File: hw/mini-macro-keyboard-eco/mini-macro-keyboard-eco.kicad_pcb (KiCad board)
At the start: 2 copper layers, 59.2 x 30.5 mm, 32 parts, among them J0 USB, J1 DEBUG_SWD, SW1 SW_Cherry_MX_1.00u_PCB, SW2 SW_Cherry_MX_1.00u_PCB, SW3 SW_Cherry_MX_1.00u_PCB, SW5 LAYOUT, SW6 BACKLIGHT, U1 USBLC6-2SC6, U2 XC6206P322MR, U3 STM32F070F6P6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

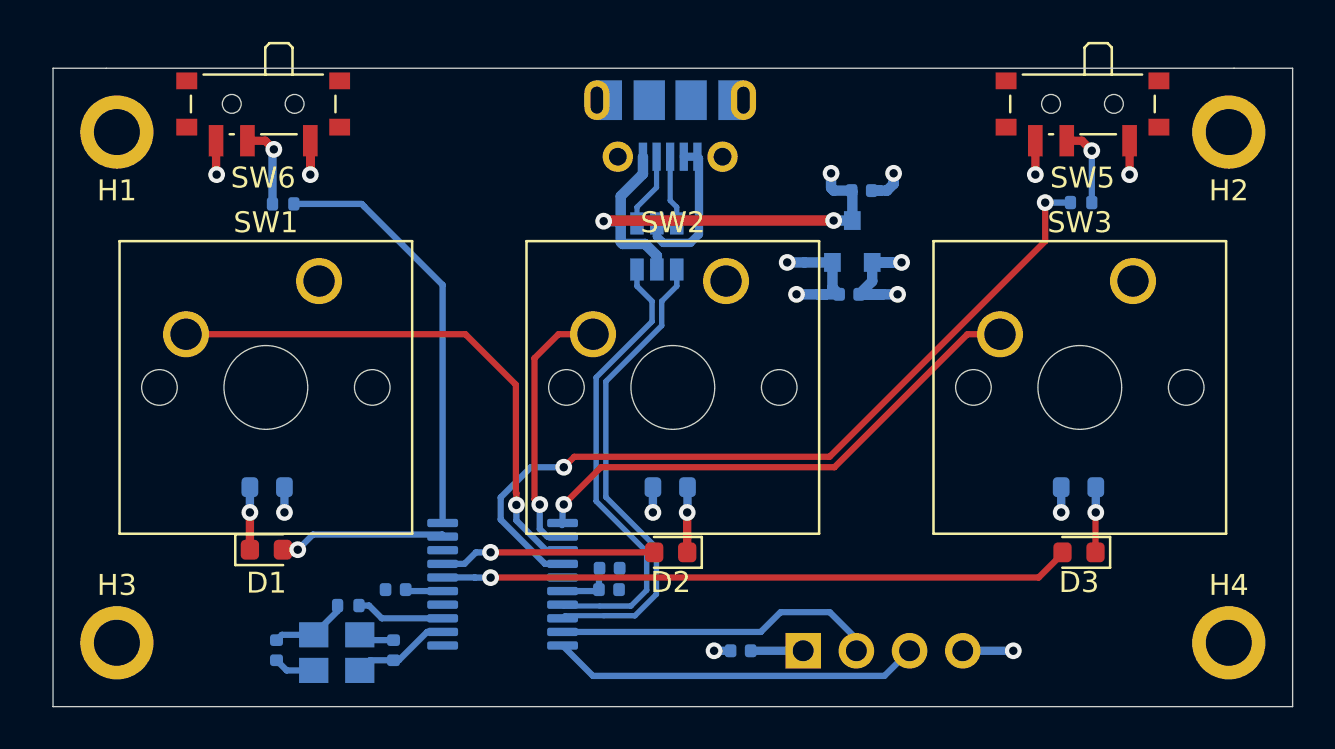
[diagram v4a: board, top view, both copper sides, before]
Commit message: feat(hw): add filled power and ground plates
Signed-off-by: Ivan Kovalenko <s1ckretbox@gmail.com>
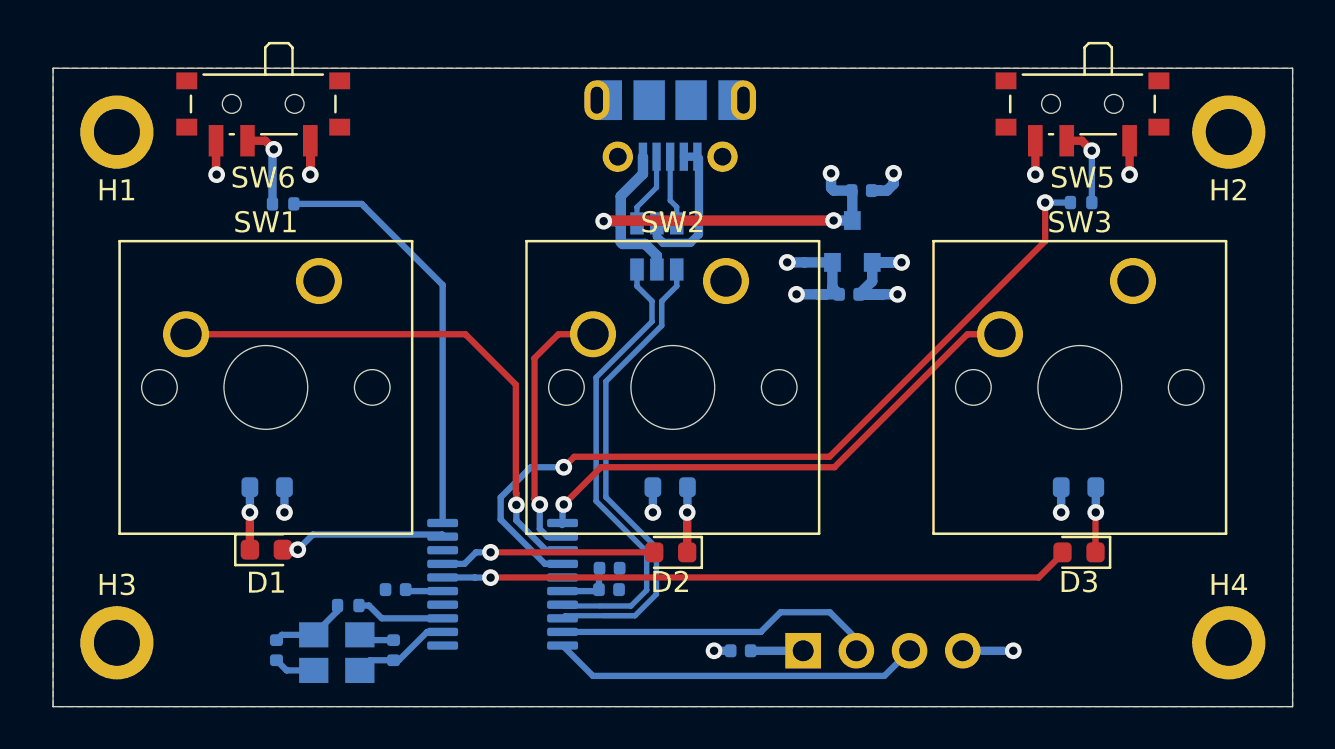
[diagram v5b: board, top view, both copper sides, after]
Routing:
- added copper zone on F.Cu, net +3V3
- added copper zone on B.Cu, net GND
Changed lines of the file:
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@@
   (segment (start 124.714 112.141) (end 124.46 112.395) (width 0.3) (layer B.Cu) (net 26))
   (segment (start 126.238 112.141) (end 124.714 112.141) (width 0.3) (layer B.Cu) (net 26))
+  (zone (net 1) (net_name GND) (layer B.Cu) (hatch edge 0.508)
+    (connect_pads (clearance 0.508))
+    (min_thickness 0.254)
+    (fill yes (arc_segments 32) (thermal_gap 0.508) (thermal_bridge_width 0.508))
+    (polygon
+      (pts
+        (xy 172.974 115.57) (xy 113.792 115.57) (xy 113.792 85.09) (xy 172.974 85.09)
+      )
+    )
+  )
+  (zone (net 2) (net_name +3V3) (layer F.Cu) (hatch edge 0.508)
+    (connect_pads (clearance 0.508))
+    (min_thickness 0.254)
+    (fill yes (arc_segments 32) (thermal_gap 0.508) (thermal_bridge_width 0.508))
+    (polygon
+      (pts
+        (xy 172.974 115.57) (xy 113.792 115.57) (xy 113.792 85.09) (xy 172.974 85.09)
+      )
+    )
+  )
 )

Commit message: feat(hw): add silkscreen
Signed-off-by: Ivan Kovalenko <s1ckretbox@gmail.com>
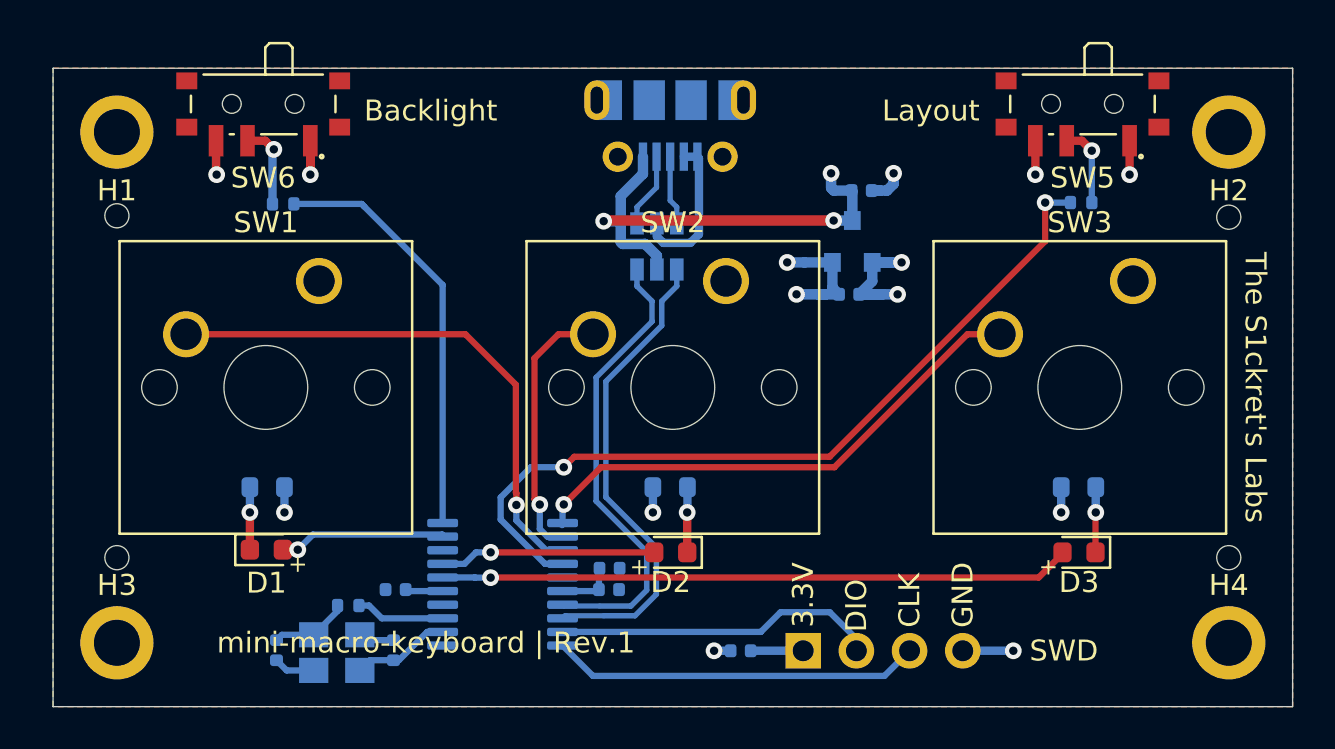
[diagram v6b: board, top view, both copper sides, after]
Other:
- outline, holes or cut-outs redrawn
- board text added: "+"
- board text added: "16 MHz"
- board text added: "3.3V"
- board text added: "Backlight"
- board text added: "CLK"
- board text added: "DIO"
- board text added: "GND"
- board text added: "JLCJLCJLC"
- board text added: "LDO"
- board text added: "Layout"
- board text added: "STM32F070F6P6"
- board text added: "SWD"
- board text added: "The S1ckret's Labs"
- board text added: "USB 2.0 FS"
- board text added: "mini-macro-keyboard | Rev.1"
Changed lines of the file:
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@@
   (general
     (thickness 1.6)
-    (drawings 6)
+    (drawings 34)
     (tracks 238)
     (zones 0)
@@
     (tags capacitor)
     (attr smd)
-    (fp_text reference C1 (at 0 1.16 270) (layer B.SilkS)
+    (fp_text reference C1 (at 0 -1.143 270) (layer B.SilkS)
       (effects (font (size 1 1) (thickness 0.15)) (justify mirror))
     )
@@
     (tags capacitor)
     (attr smd)
-    (fp_text reference C0 (at 0 1.16 270) (layer B.SilkS)
+    (fp_text reference C0 (at 1.298 -1.27 270) (layer B.SilkS)
       (effects (font (size 1 1) (thickness 0.15)) (justify mirror))
     )
@@
     (tags "SMD SMT crystal")
     (attr smd)
-    (fp_text reference Y1 (at 0 2.45) (layer B.SilkS)
+    (fp_text reference Y1 (at 1.608 2.45) (layer B.SilkS)
       (effects (font (size 1 1) (thickness 0.15)) (justify mirror))
     )
@@
     )
   )
+  (gr_circle (center 116.84 92.134) (end 117.416 92.134) (layer Edge.Cuts) (width 0.05))
+  (gr_circle (center 116.84 108.458) (end 117.416 108.458) (layer Edge.Cuts) (width 0.05))
+  (gr_circle (center 169.926 92.202) (end 170.502 92.202) (layer Edge.Cuts) (width 0.05))
+  (gr_circle (center 169.926 108.458) (end 170.502 108.458) (layer Edge.Cuts) (width 0.05))
+  (gr_text JLCJLCJLC (at 135.89 109.728 90) (layer B.SilkS)
+    (effects (font (size 0.8 0.8) (thickness 0.15)) (justify mirror))
+  )
+  (gr_text "The S1ckret's Labs" (at 171.196 100.33 270) (layer F.SilkS)
+    (effects (font (size 1 1) (thickness 0.15)))
+  )
+  (gr_text "mini-macro-keyboard | Rev.1" (at 131.5974 112.522) (layer F.SilkS)
+    (effects (font (size 1 1) (thickness 0.15)))
+  )
+  (gr_text + (at 161.3154 108.8898) (layer F.SilkS)
+    (effects (font (size 0.8 0.8) (thickness 0.1)))
+  )
+  (gr_text + (at 141.7828 108.8898) (layer F.SilkS)
+    (effects (font (size 0.8 0.8) (thickness 0.1)))
+  )
+  (gr_text + (at 125.476 108.7628) (layer F.SilkS)
+    (effects (font (size 0.8 0.8) (thickness 0.1)))
+  )
+  (gr_circle (center 128.524 114.9604) (end 128.524 115.062) (layer B.SilkS) (width 0.12))
+  (gr_circle (center 131.0386 112.649) (end 131.0386 112.7252) (layer B.SilkS) (width 0.12))
+  (gr_circle (center 152.908 95.1992) (end 152.9334 95.2754) (layer B.SilkS) (width 0.12))
+  (gr_circle (center 141.7066 91.694) (end 141.7066 91.6178) (layer B.SilkS) (width 0.12))
+  (gr_circle (center 141.9606 90.4748) (end 141.9606 90.551) (layer B.SilkS) (width 0.12))
+  (gr_circle (center 165.735 89.3064) (end 165.7604 89.3826) (layer F.SilkS) (width 0.12))
+  (gr_circle (center 126.619 89.3064) (end 126.6444 89.3826) (layer F.SilkS) (width 0.12))
+  (gr_text "USB\n2.0 FS\n" (at 136.271 87.122) (layer B.SilkS)
+    (effects (font (size 1 1) (thickness 0.15)) (justify mirror))
+  )
+  (gr_text LDO (at 157.353 93.345) (layer B.SilkS)
+    (effects (font (size 1.5 1.5) (thickness 0.2)) (justify mirror))
+  )
+  (gr_text "16\nMHz" (at 120.904 112.395) (layer B.SilkS)
+    (effects (font (size 1 1) (thickness 0.15)) (justify mirror))
+  )
+  (gr_text STM32F070F6P6 (at 130.81 105.664) (layer B.SilkS)
+    (effects (font (size 0.75 0.75) (thickness 0.1)) (justify mirror))
+  )
+  (gr_text SWD (at 162.052 112.903) (layer F.SilkS)
+    (effects (font (size 1 1) (thickness 0.15)))
+  )
+  (gr_text 3.3V (at 149.606 110.236 90) (layer F.SilkS)
+    (effects (font (size 1 1) (thickness 0.15)))
+  )
+  (gr_text GND (at 157.226 110.236 90) (layer F.SilkS)
+    (effects (font (size 1 1) (thickness 0.15)))
+  )
+  (gr_text DIO (at 152.146 110.744 90) (layer F.SilkS)
+    (effects (font (size 1 1) (thickness 0.15)))
+  )
+  (gr_text CLK (at 154.686 110.49 90) (layer F.SilkS)
+    (effects (font (size 1 1) (thickness 0.15)))
+  )
+  (gr_text Layout (at 155.702 87.122) (layer F.SilkS)
+    (effects (font (size 1 1) (thickness 0.15)))
+  )
+  (gr_text Backlight (at 131.826 87.122) (layer F.SilkS)
+    (effects (font (size 1 1) (thickness 0.15)))
+  )
   (gr_line (start 113.792 85.09) (end 116.332 85.09) (layer Edge.Cuts) (width 0.05))
